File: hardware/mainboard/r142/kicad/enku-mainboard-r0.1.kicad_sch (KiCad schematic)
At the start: 0 parts

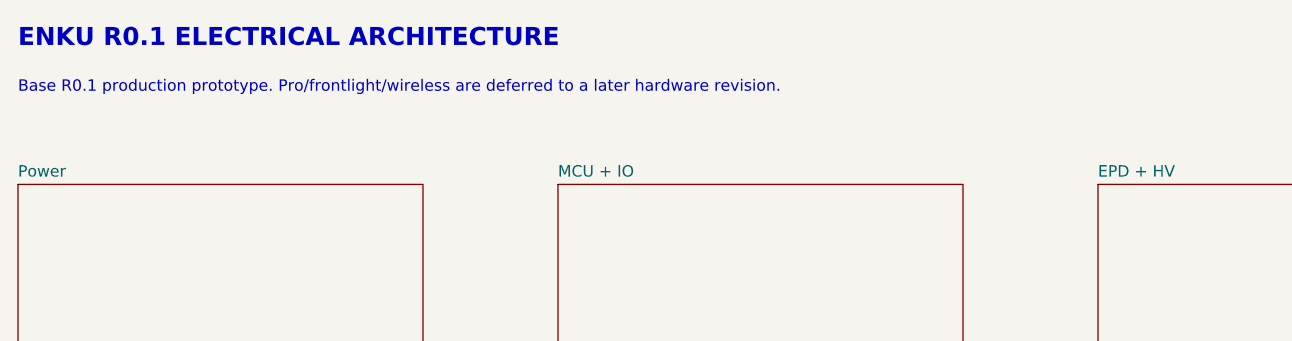
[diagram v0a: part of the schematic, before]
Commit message: R142: separate SD schematic group and refresh engineering notes; preserve electrical graph
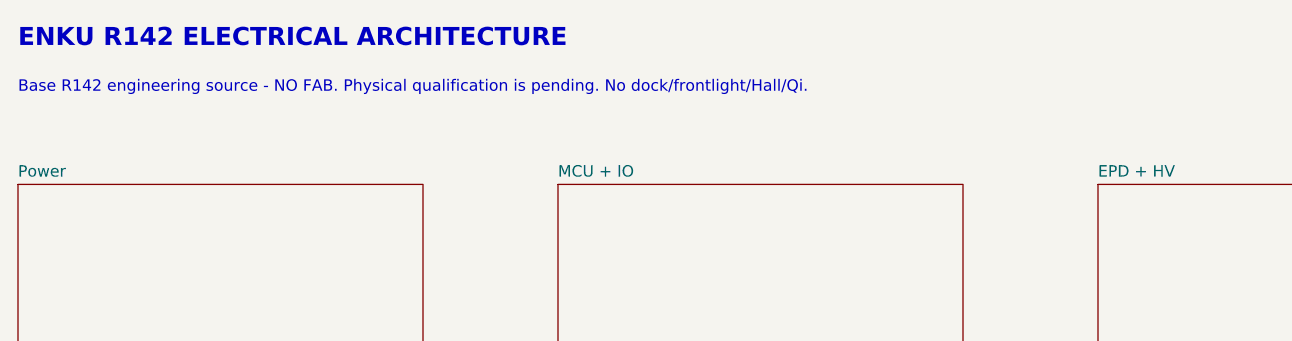
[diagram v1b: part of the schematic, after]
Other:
- note added: "Base R142 engineering source - NO FAB. Physical qualification is pending. No dock/frontlight/Hall/Qi."
- note added: "ENKU R142 ELECTRICAL ARCHITECTURE"
- note removed: "Base R0.1 production prototype. Pro/frontlight/wireless are deferred to a later hardware revision."
- note removed: "ENKU R0.1 ELECTRICAL ARCHITECTURE"
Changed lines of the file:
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@@
 		)
 	)
-	(text "ENKU R0.1 ELECTRICAL ARCHITECTURE" (exclude_from_sim no) (at 25 20 0)
+	(text "ENKU R142 ELECTRICAL ARCHITECTURE" (exclude_from_sim no) (at 25 20 0)
 		(effects (font (size 2 2) (bold yes)) (justify left bottom))
 	)
-	(text "Base R0.1 production prototype. Pro/frontlight/wireless are deferred to a later hardware revision." (exclude_from_sim no) (at 25 25 0)
+	(text "Base R142 engineering source - NO FAB. Physical qualification is pending. No dock/frontlight/Hall/Qi." (exclude_from_sim no) (at 25 25 0)
 		(effects (font (size 1.27 1.27)) (justify left bottom))
 	)
